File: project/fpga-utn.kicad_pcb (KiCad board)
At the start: 2 copper layers, 100 x 75 mm, 154 parts, among them J1 USB_C_Receptacle_USB2.0_16P, P1 Conector 2x10, P2 Conector 2x10, P3 Conector 2x10, P4 Conector 2x10, SW1 SW_Push, SW2 SW_Push, SW3 SW_Push, SW4 SW_Push, SW5 SW_Push, SW6 SW_Push, SW7 SW_Push, SW8 SW_Push, U1 LD1117S33CTR, U2 LD1117S12CTR, U3 USBLC6-2SC6, U4 FT2232HL, U5 M93C66, U6 ICE40HX4K-TQ144, U7 W25X40CLSN, Y1 ECS-3225MV-120-CN-TR, Y2 ECS-3225MVQ-1000-CN-TR

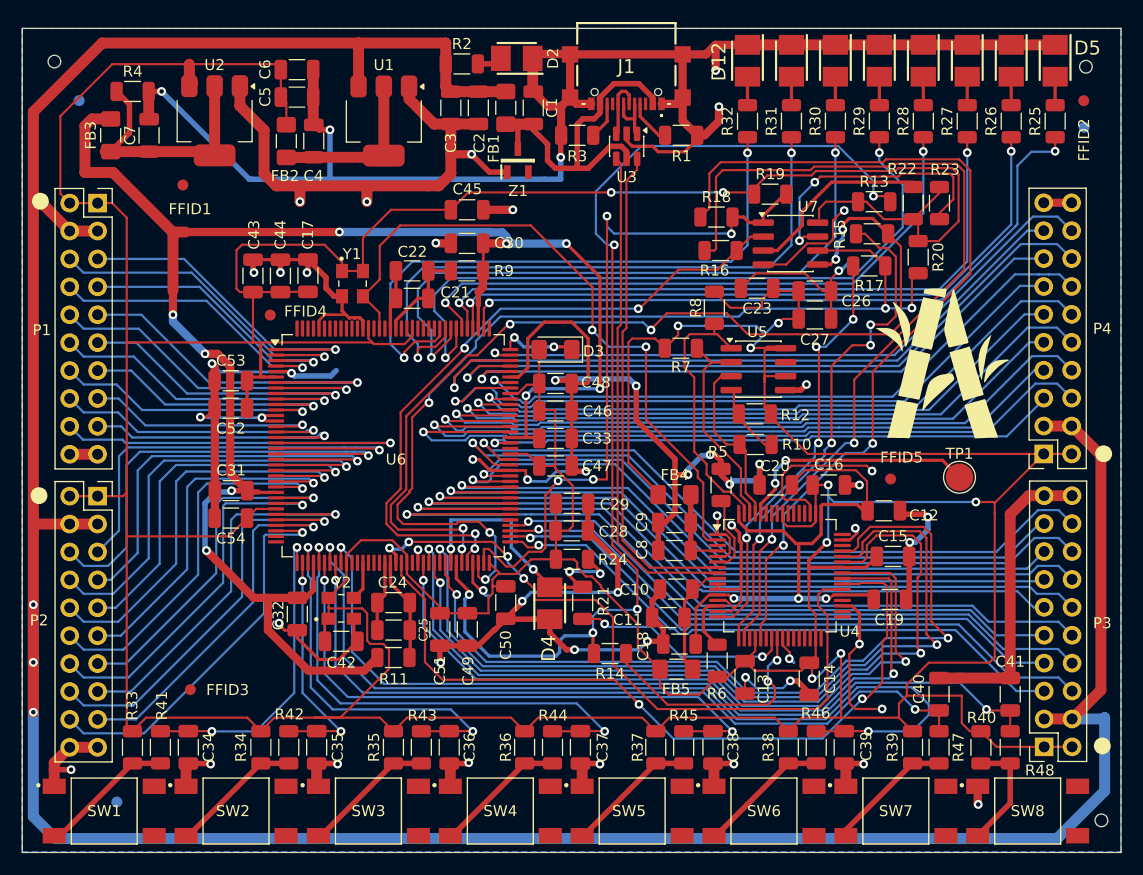
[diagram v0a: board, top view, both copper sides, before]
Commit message: pista de linea 3v3 ampliada
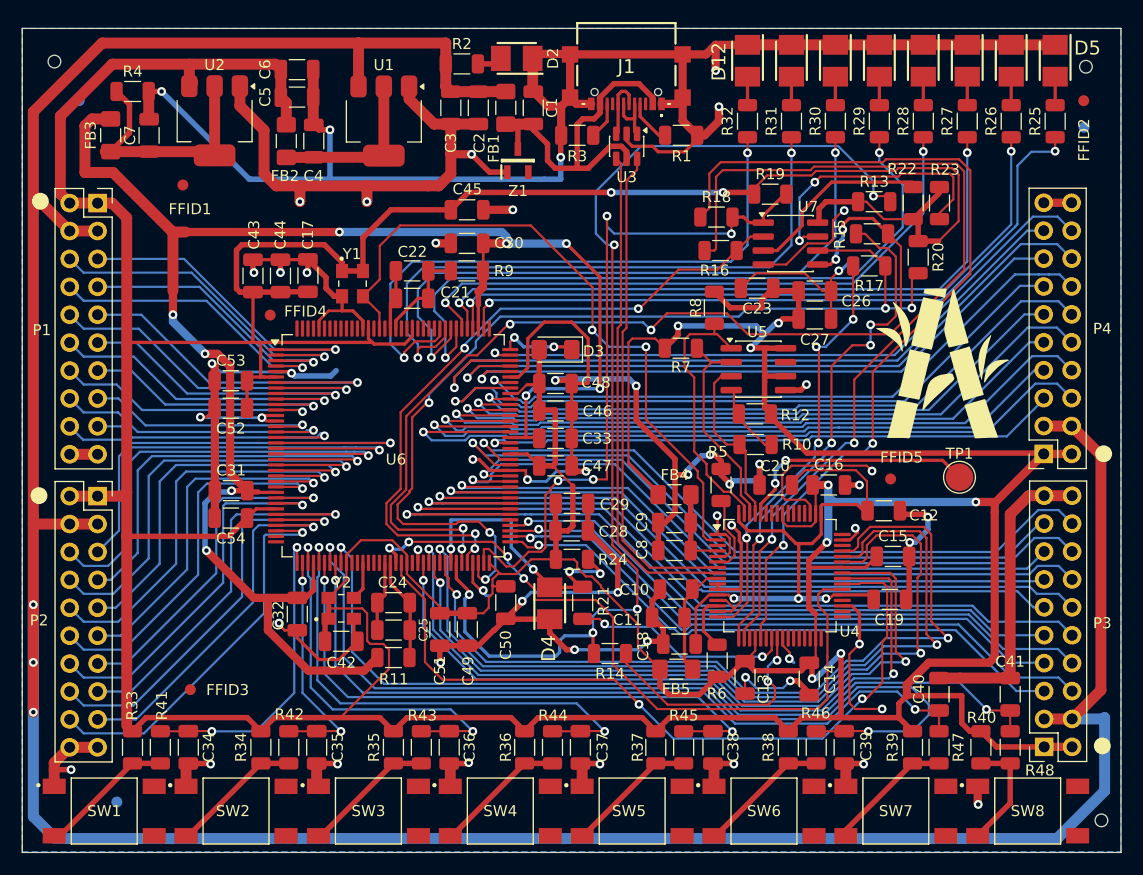
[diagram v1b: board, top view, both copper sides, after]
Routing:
- net +3V3: track 665.5 -> 663.5 mm

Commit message: Correciones de pistas varias, sacando una pista entre pads de la eeprom, ordenamiento de algunas vias, cambio de cristal de 12mhz al lado del ftdi, etc
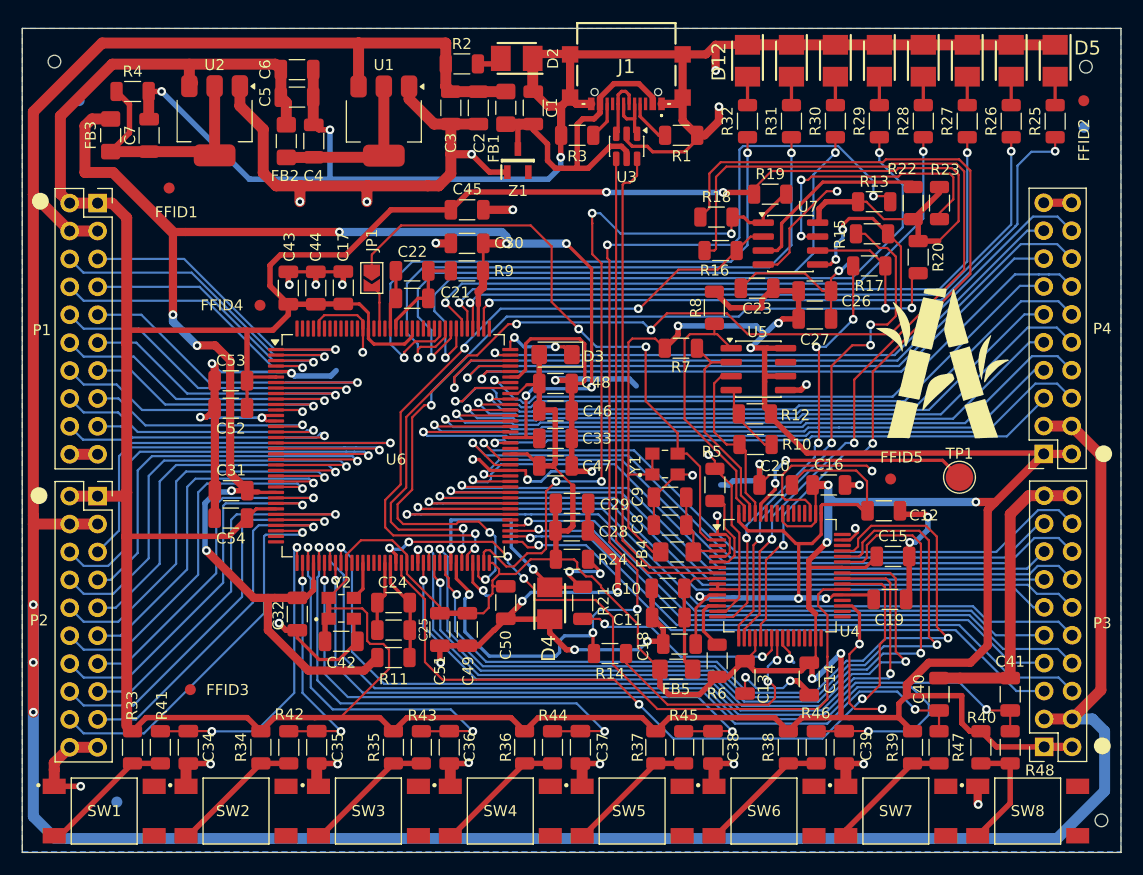
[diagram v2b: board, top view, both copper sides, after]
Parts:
- added JP1: SolderJumper_2_Open, Jumper:SolderJumper-2_P1.3mm_Open_TrianglePad1.0x1.5mm, F.Cu at (151.8, 92.7)
- moved Y1 32.8 mm to (178.5, 109.7), turned to 0 degrees
- moved FB4 5.22 mm to (179.6, 117.7)
- moved C17 3.40 mm to (149.2, 93.6)
- moved C43 3.40 mm to (144.2, 93.6)
- moved C44 3.40 mm to (146.7, 93.6)
- moved C8 2.34 mm to (179.0, 115.2)
- moved C9 2.34 mm to (179.0, 112.7)
- moved FFID4 1.29 mm to (141.6, 95.2)
- moved FFID1 1.28 mm to (133.4, 84.5)
- moved C10 0.75 mm to (178.8, 121.0)
- moved R5 0.56 mm to (183.0, 111.5)
- moved D3 0.46 mm to (168.5, 99.7)
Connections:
- U6 pad 129: /Perifericos/12MHz_CLK -> Net-(JP1-B)
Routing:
- net GND: track 572.6 -> 559.2 mm, vias 57 -> 55
- net /Perifericos/12MHz_CLK: track 61.5 -> 56.3 mm
- net +3V3: track 663.5 -> 658.6 mm
- net Net-(JP1-B): track 0.00 -> 4.17 mm
- net +1V8: track 51.3 -> 53.9 mm
- net Net-(U6E-IOB_108_SS): track 63.9 -> 65.0 mm
- net +1V2: track 159.6 -> 158.8 mm
- net +5V: track 284.4 -> 283.6 mm
- net Net-(U2-VO): track 23.1 -> 22.6 mm
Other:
- board text added: "VERSION 1.4 © 2026"
- board text removed: "VERSION 1.3 © 2026"

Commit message: Agregada licencia CERN-OHL-P-2.0
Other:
- board text added: "AZUKAR FPGA Version 1.4 - 2026 CERN-OHL-P-2.0 © M. Simonazzi, V. Gomez Espeche"
- board text removed: "VERSION 1.4 © 2026"
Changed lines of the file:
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@@
+		)
+	)
+	(gr_text "AZUKAR FPGA Version 1.4 - 2026\nCERN-OHL-P-2.0\n© M. Simonazzi, V. Gomez Espeche"
+		(at 163.24 142.56 0)
+		(layer "B.SilkS")
+		(effects
+			(font
+				(size 1 1)
+				(thickness 0.2)
+				(bold yes)
+			)
+			(justify left bottom mirror)
 		)
 	)
@@
 			)
 			(justify left bottom mirror)
-		)
-	)
-	(gr_text "VERSION 1.4 © 2026"
-		(at 164.29 141.87 0)
-		(layer "B.SilkS")
-		(effects
-			(font
-				(size 2 2)
-				(thickness 0.4)
-				(bold yes)
-			)
-			(justify left bottom mirror)
